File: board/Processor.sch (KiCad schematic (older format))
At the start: 1 part, among them U1 TM4C123GH6PM

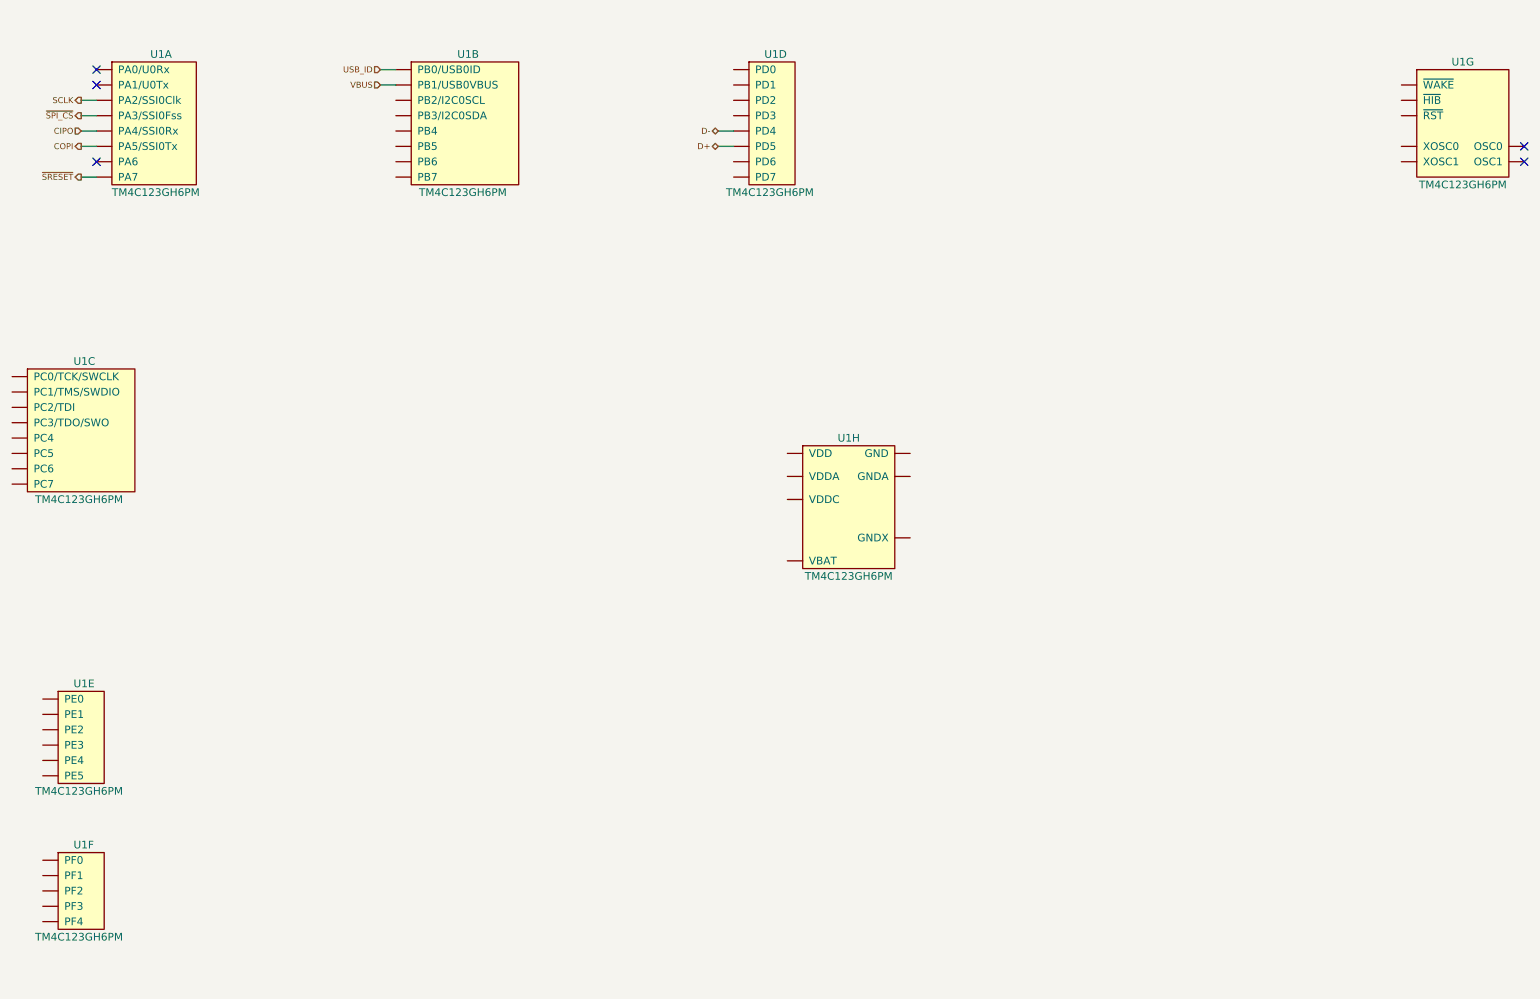
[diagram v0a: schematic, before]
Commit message: Added in JTAG connections to the processor
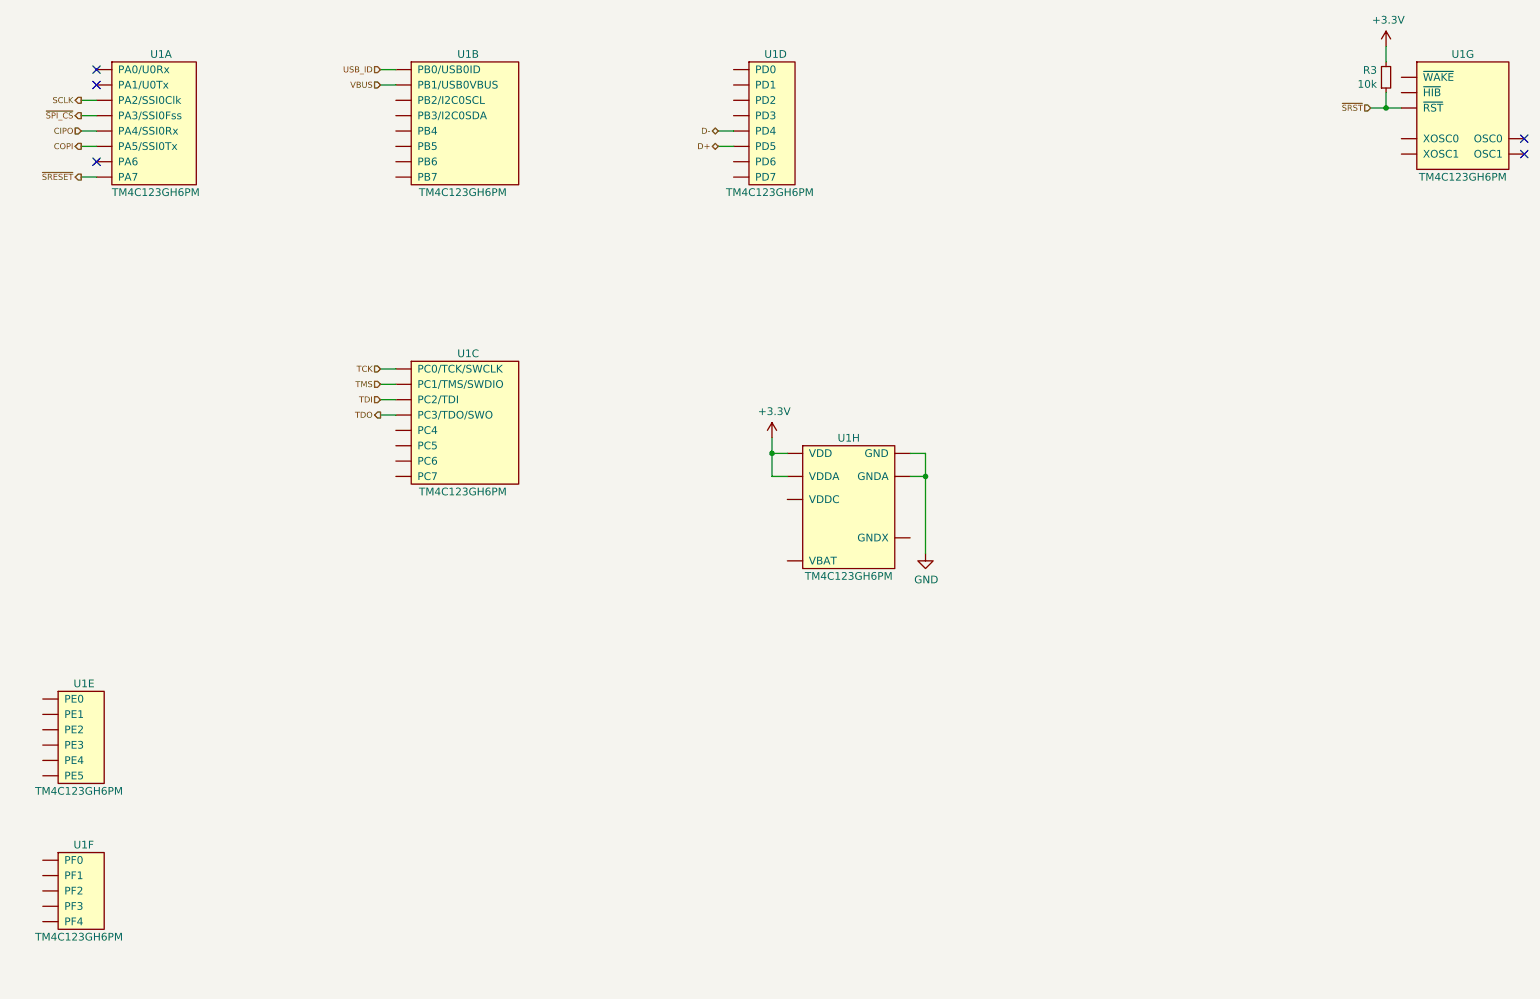
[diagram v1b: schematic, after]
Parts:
- added R3: 10k, rcl:R0603, symbol Device:R_Small
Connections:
- net TDO: now reaches U1.49 (PC3/TDO/SWO)
- net TDI: now reaches U1.50 (PC2/TDI)
- net TMS: now reaches U1.51 (PC1/TMS/SWDIO)
- net TCK: now reaches U1.52 (PC0/TCK/SWCLK)
- net ~SRST: now reaches U1.38 (~RST)
- net ~SRST: now also R3.1
- net +3V3: now reaches U1.11 (VDD), U1.26 (VDD), U1.42 (VDD), U1.54 (VDD)
- net +3V3: now also U1.2 (VDDA), R3.2
- net GND: now reaches U1.12 (GND), U1.27 (GND), U1.39 (GND), U1.55 (GND)
- net GND: now also U1.3 (GNDA)
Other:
- moved on the sheet: U1C, U1G
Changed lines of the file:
@@
 L DX_MON:TM4C123GH6PM U1
 U 3 1 5F0AE054
-P 1500 3500
-F 0 "U1" H 1450 3950 50  0000 L CNN
-F 1 "TM4C123GH6PM" H 1200 3050 50  0000 L CNN
-F 2 "DX-MON:QFP-64_10.2x10.2_Pitch0.5mm" H 1450 3500 50  0001 C CNN
-F 3 "" H 1450 3500 50  0001 C CNN
-F 4 "3008366" H 1500 2850 50  0001 C CNN "OC_FARNELL"
-F 5 "https://uk.farnell.com/texas-instruments/tm4c123gh6pmi/mcu-32bit-cortex-m4f-80mhz-lqfp/dp/3008366" H 1500 2950 50  0001 C CNN "URL_FARNELL"
-F 6 "Texas Instruments" H 1500 4050 50  0001 C CNN "MFR"
-F 7 "TM4C123GH6PM" H 1500 3950 50  0001 C CNN "MPN"
-	3    1500 3500
+P 4000 3450
+F 0 "U1" H 3950 3900 50  0000 L CNN
+F 1 "TM4C123GH6PM" H 3700 3000 50  0000 L CNN
+F 2 "DX-MON:QFP-64_10.2x10.2_Pitch0.5mm" H 3950 3450 50  0001 C CNN
+F 3 "" H 3950 3450 50  0001 C CNN
+F 4 "3008366" H 4000 2800 50  0001 C CNN "OC_FARNELL"
+F 5 "https://uk.farnell.com/texas-instruments/tm4c123gh6pmi/mcu-32bit-cortex-m4f-80mhz-lqfp/dp/3008366" H 4000 2900 50  0001 C CNN "URL_FARNELL"
+F 6 "Texas Instruments" H 4000 4000 50  0001 C CNN "MFR"
+F 7 "TM4C123GH6PM" H 4000 3900 50  0001 C CNN "MPN"
+	3    4000 3450
 	1    0    0    -1
 $EndComp
@@
 L DX_MON:TM4C123GH6PM U1
 U 7 1 5F0B8450
-P 10500 1500
-F 0 "U1" H 10500 1900 50  0000 C CNN
-F 1 "TM4C123GH6PM" H 10500 1100 50  0000 C CNN
-F 2 "DX-MON:QFP-64_10.2x10.2_Pitch0.5mm" H 10450 1500 50  0001 C CNN
-F 3 "" H 10450 1500 50  0001 C CNN
-F 4 "3008366" H 10500 850 50  0001 C CNN "OC_FARNELL"
-F 5 "https://uk.farnell.com/texas-instruments/tm4c123gh6pmi/mcu-32bit-cortex-m4f-80mhz-lqfp/dp/3008366" H 10500 950 50  0001 C CNN "URL_FARNELL"
-F 6 "Texas Instruments" H 10500 2050 50  0001 C CNN "MFR"
-F 7 "TM4C123GH6PM" H 10500 1950 50  0001 C CNN "MPN"
-	7    10500 1500
+P 10500 1450
+F 0 "U1" H 10500 1850 50  0000 C CNN
+F 1 "TM4C123GH6PM" H 10500 1050 50  0000 C CNN
+F 2 "DX-MON:QFP-64_10.2x10.2_Pitch0.5mm" H 10450 1450 50  0001 C CNN
+F 3 "" H 10450 1450 50  0001 C CNN
+F 4 "3008366" H 10500 800 50  0001 C CNN "OC_FARNELL"
+F 5 "https://uk.farnell.com/texas-instruments/tm4c123gh6pmi/mcu-32bit-cortex-m4f-80mhz-lqfp/dp/3008366" H 10500 900 50  0001 C CNN "URL_FARNELL"
+F 6 "Texas Instruments" H 10500 2000 50  0001 C CNN "MFR"
+F 7 "TM4C123GH6PM" H 10500 1900 50  0001 C CNN "MPN"
+	7    10500 1450
 	1    0    0    -1
 $EndComp
@@
 Text HLabel 5650 1650 0    39   BiDi ~ 0
 D+
-NoConn ~ 10900 1650
-NoConn ~ 10900 1750
+NoConn ~ 10900 1600
+NoConn ~ 10900 1700
+Text HLabel 3450 3100 0    39   Input ~ 0
+TCK
+Text HLabel 3450 3200 0    39   Input ~ 0
+TMS
+Text HLabel 3450 3300 0    39   Input ~ 0
+TDI
+Text HLabel 3450 3400 0    39   Output ~ 0
+TDO
+Wire Wire Line
+	3450 3100 3550 3100
+Wire Wire Line
+	3550 3200 3450 3200
+Wire Wire Line
+	3450 3300 3550 3300
+Wire Wire Line
+	3550 3400 3450 3400
+Wire Wire Line
+	10100 1400 10000 1400
+Text HLabel 9900 1400 0    39   Input ~ 0
+~SRST
+$Comp
+L Device:R_Small R3
+U 1 1 5F504ECC
+P 10000 1200
+F 0 "R3" H 9941 1154 50  0000 R CNN
+F 1 "10k" H 9941 1245 50  0000 R CNN
+F 2 "rcl:R0603" H 10000 1200 50  0001 C CNN
+F 3 "~" H 10000 1200 50  0001 C CNN
+	1    10000 1200
+	1    0    0    1
+$EndComp
+$Comp
+L power:GND #PWR011
+U 1 1 5F5057F5
+P 7000 4300
+F 0 "#PWR011" H 7000 4050 50  0001 C CNN
+F 1 "GND" H 7005 4127 50  0000 C CNN
+F 2 "" H 7000 4300 50  0001 C CNN
+F 3 "" H 7000 4300 50  0001 C CNN
+	1    7000 4300
+	1    0    0    -1
+$EndComp
+$Comp
+L power:+3.3V #PWR07
+U 1 1 5F5063F5
+P 6000 3550
+F 0 "#PWR07" H 6000 3400 50  0001 C CNN
+F 1 "+3.3V" H 6015 3723 50  0000 C CNN
+F 2 "" H 6000 3550 50  0001 C CNN
+F 3 "" H 6000 3550 50  0001 C CNN
+	1    6000 3550
+	1    0    0    -1
+$EndComp
+Wire Wire Line
+	6000 3550 6000 3650
+Wire Wire Line
+	6000 3650 6100 3650
+Wire Wire Line
+	6900 3650 7000 3650
+Wire Wire Line
+	7000 3650 7000 3800
+Wire Wire Line
+	6900 3800 7000 3800
+Connection ~ 7000 3800
+Wire Wire Line
+	7000 3800 7000 4300
+Wire Wire Line
+	6100 3800 6000 3800
+Wire Wire Line
+	6000 3800 6000 3650
+Connection ~ 6000 3650
+$Comp
+L power:+3.3V #PWR012
+U 1 1 5F509B63
+P 10000 1000
+F 0 "#PWR012" H 10000 850 50  0001 C CNN
+F 1 "+3.3V" H 10015 1173 50  0000 C CNN
+F 2 "" H 10000 1000 50  0001 C CNN
+F 3 "" H 10000 1000 50  0001 C CNN
+	1    10000 1000
+	1    0    0    -1
+$EndComp
+Wire Wire Line
+	10000 1300 10000 1400
+Connection ~ 10000 1400
+Wire Wire Line
+	10000 1400 9900 1400
+Wire Wire Line
+	10000 1100 10000 1000
 $EndSCHEMATC

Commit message: Added the work to the schematic from the last stream, and updated all the footprints to reflect the work going in on my symbol and footprint libraries
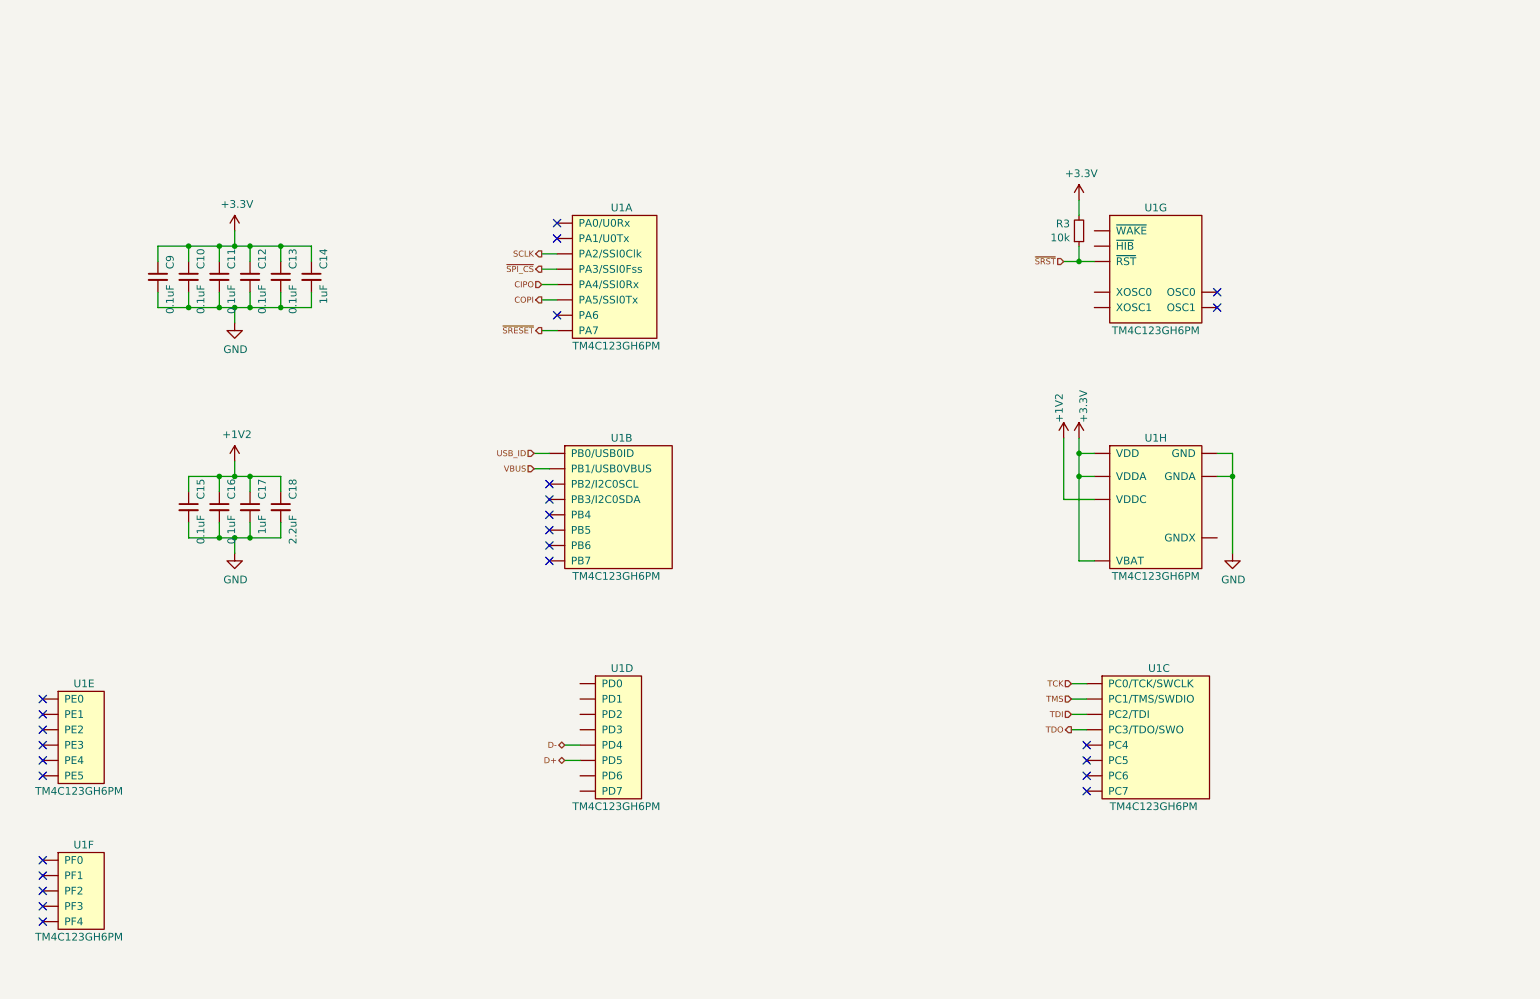
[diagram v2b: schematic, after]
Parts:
- added C10, C11, C12, C13, C15, C16, C9: 0.1uF, rhais_rcl:C0603, symbol Device:C_Small
- added C14, C17: 1uF, rhais_rcl:C0603, symbol Device:C_Small
- added C18: 2.2uF, rhais_rcl:C0603, symbol Device:C_Small
- R3: footprint rcl:R0603 -> rhais_rcl:R0603
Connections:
- net +3V3: now also U1.37 (VBAT), C10.1, C11.1, C12.1, C13.1, C14.1, C9.1
- net GND: now also C10.2, C11.2, C12.2, C13.2, C14.2, C15.2, C16.2, C17.2, C18.2, C9.2
- net +1V2: now reaches U1.25 (VDDC), U1.56 (VDDC)
- net +1V2: now also C15.1, C16.1, C17.1, C18.1
- no-connect marks 5 -> 26
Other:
- moved on the sheet: R3, U1A, U1B, U1C, U1D, U1G, U1H
